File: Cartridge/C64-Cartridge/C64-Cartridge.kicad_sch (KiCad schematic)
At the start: 22 parts, among them J1 C64_Expansion_port, J2 GND, SW1 SW_DIP_x08, SW2 RESET, SW3 RESET, U1 SST39SF040

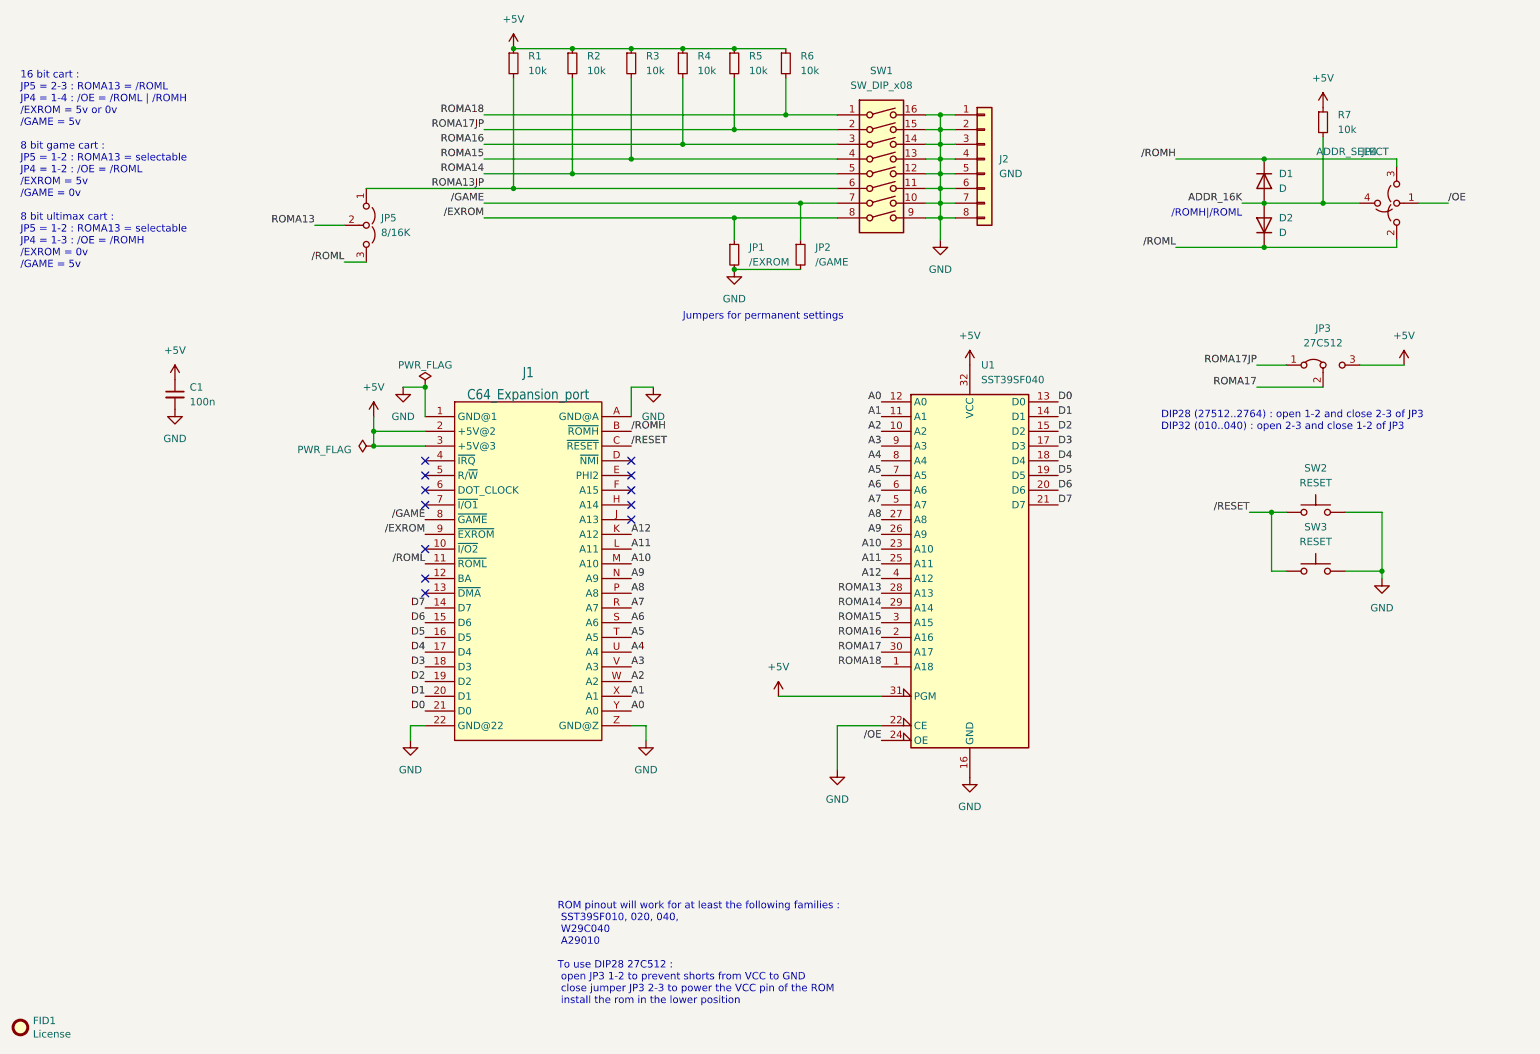
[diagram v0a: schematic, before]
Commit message: C64-Cartridge : addition of EpyxFastload daughter board ; some silkscreen changes. C64-KungFuFlash, C64-Pi1541 : small updates before production. New C64-efuse board that fit inside the DIN plug.
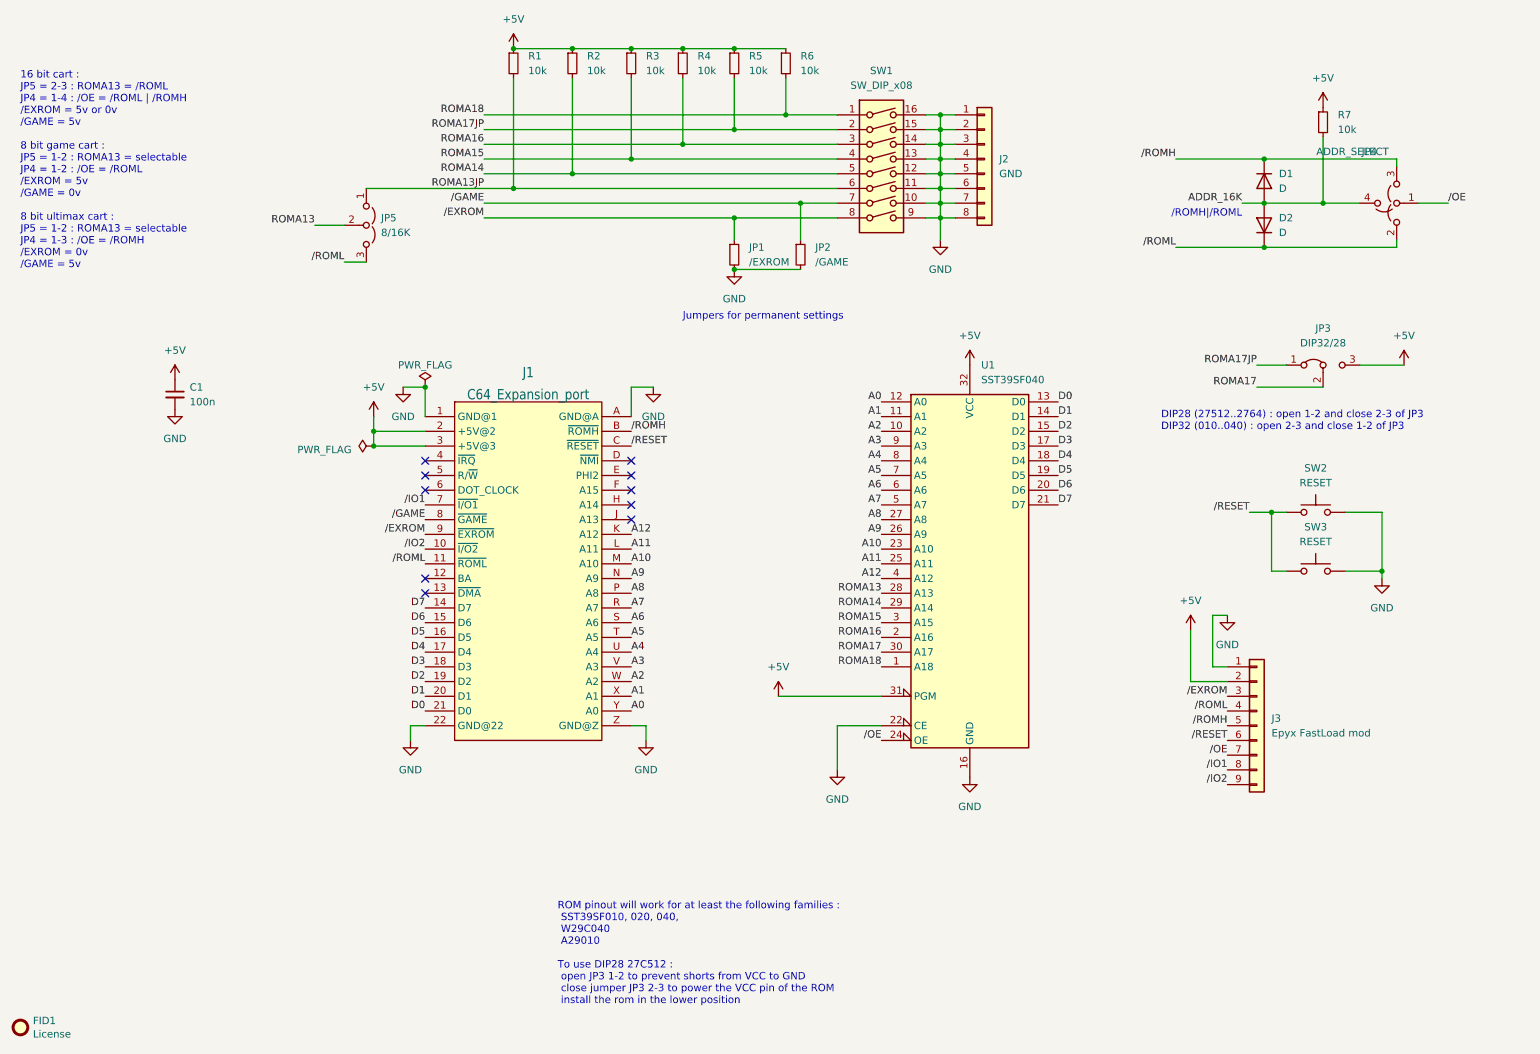
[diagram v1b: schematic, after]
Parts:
- added J3: Epyx FastLoad mod, Connector_PinHeader_1.27mm:PinHeader_1x09_P1.27mm_Vertical, symbol Connector_Generic:Conn_01x09
- JP3: value 27C512 -> DIP32/28; footprint Jumper:SolderJumper-3_P1.3mm_Bridged12_RoundedPad1.0x1.5mm -> Jumper:SolderJumper-3_P1.3mm_Open_RoundedPad1.0x1.5mm
- R1, R2, R3: footprint Sassa:C_0805_2012Metric_shortable -> Resistor_SMD:R_0805_2012Metric
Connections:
- net +5V: now also J3.2 (Pin_2)
- net GND: now also J3.1 (Pin_1)
- net /EXROM: now also J3.3 (Pin_3)
- net /OE: now also J3.7 (Pin_7)
- net /RESET: now also J3.6 (Pin_6)
- net /ROMH: now also J3.5 (Pin_5)
- net /ROML: now also J3.4 (Pin_4)
- net /IO2: now reaches J1.10 (~{I/O2})
- net /IO2: now also J3.9 (Pin_9)
- net /IO1: now reaches J1.7 (~{I/O1})
- net /IO1: now also J3.8 (Pin_8)
- no-connect marks 12 -> 10
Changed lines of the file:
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@@
   (junction (at 124.46 41.91) (diameter 0) (color 0 0 0 0)
   )
-  (no_connect (at 88.9 101.6))
   (no_connect (at 88.9 99.06))
   (no_connect (at 124.46 96.52))
-  (no_connect (at 88.9 109.22))
   (no_connect (at 88.9 93.98))
   (no_connect (at 88.9 116.84))
@@
     (stroke (width 0) (type default))
   )
+  (wire (pts (xy 227.33 129.54) (xy 224.79 129.54))
+    (stroke (width 0) (type default))
+  )
   (wire (pts (xy 177.8 44.45) (xy 180.34 44.45))
     (stroke (width 0) (type default))
@@
     (stroke (width 0) (type default))
   )
+  (wire (pts (xy 224.79 120.65) (xy 227.33 120.65))
+    (stroke (width 0) (type default))
+  )
   (wire (pts (xy 160.02 139.7) (xy 160.02 147.32))
     (stroke (width 0) (type default))
@@
     (stroke (width 0) (type default))
   )
+  (wire (pts (xy 224.79 129.54) (xy 224.79 120.65))
+    (stroke (width 0) (type default))
+  )
   (wire (pts (xy 260.35 49.53) (xy 265.43 49.53))
     (stroke (width 0) (type default))
@@
     (stroke (width 0) (type default))
   )
+  (wire (pts (xy 220.98 132.08) (xy 220.98 123.19))
+    (stroke (width 0) (type default))
+  )
   (wire (pts (xy 247.65 113.03) (xy 254 113.03))
     (stroke (width 0) (type default))
@@
   )
   (wire (pts (xy 124.46 41.91) (xy 160.02 41.91))
+    (stroke (width 0) (type default))
+  )
+  (wire (pts (xy 227.33 132.08) (xy 220.98 132.08))
     (stroke (width 0) (type default))
   )
@@
     (effects (font (size 1.27 1.27)) (justify right bottom))
   )
+  (label "{slash}IO1" (at 227.33 147.32 180) (fields_autoplaced)
+    (effects (font (size 1.27 1.27)) (justify right bottom))
+  )
   (label "A7" (at 167.64 101.6 180) (fields_autoplaced)
     (effects (font (size 1.27 1.27)) (justify right bottom))
@@
     (effects (font (size 1.27 1.27)) (justify right bottom))
   )
+  (label "{slash}ROML" (at 227.33 137.16 180) (fields_autoplaced)
+    (effects (font (size 1.27 1.27)) (justify right bottom))
+  )
+  (label "{slash}IO2" (at 227.33 149.86 180) (fields_autoplaced)
+    (effects (font (size 1.27 1.27)) (justify right bottom))
+  )
   (label "A12" (at 167.64 114.3 180) (fields_autoplaced)
     (effects (font (size 1.27 1.27)) (justify right bottom))
   )
+  (label "{slash}OE" (at 227.33 144.78 180) (fields_autoplaced)
+    (effects (font (size 1.27 1.27)) (justify right bottom))
+  )
+  (label "{slash}IO1" (at 88.9 101.6 180) (fields_autoplaced)
+    (effects (font (size 1.27 1.27)) (justify right bottom))
+  )
   (label "D7" (at 198.12 101.6 0) (fields_autoplaced)
     (effects (font (size 1.27 1.27)) (justify left bottom))
@@
     (effects (font (size 1.27 1.27)) (justify left bottom))
   )
+  (label "{slash}RESET" (at 227.33 142.24 180) (fields_autoplaced)
+    (effects (font (size 1.27 1.27)) (justify right bottom))
+  )
   (label "{slash}EXROM" (at 88.9 106.68 180) (fields_autoplaced)
     (effects (font (size 1.27 1.27)) (justify right bottom))
@@
     (effects (font (size 1.27 1.27)) (justify right bottom))
   )
+  (label "{slash}ROMH" (at 227.33 139.7 180) (fields_autoplaced)
+    (effects (font (size 1.27 1.27)) (justify right bottom))
+  )
   (label "ROMA17JP" (at 232.41 77.47 180) (fields_autoplaced)
     (effects (font (size 1.27 1.27)) (justify right bottom))
   )
+  (label "{slash}IO2" (at 88.9 109.22 180) (fields_autoplaced)
+    (effects (font (size 1.27 1.27)) (justify right bottom))
+  )
   (label "D6" (at 198.12 99.06 0) (fields_autoplaced)
     (effects (font (size 1.27 1.27)) (justify left bottom))
@@
     (effects (font (size 1.27 1.27)) (justify left bottom))
   )
+  (label "{slash}EXROM" (at 227.33 134.62 180) (fields_autoplaced)
+    (effects (font (size 1.27 1.27)) (justify right bottom))
+  )
   (label "ROMA13" (at 167.64 116.84 180) (fields_autoplaced)
     (effects (font (size 1.27 1.27)) (justify right bottom))
@@
   (label "A2" (at 167.64 88.9 180) (fields_autoplaced)
     (effects (font (size 1.27 1.27)) (justify right bottom))
+  )
+  (symbol (lib_id "power:GND") (at 227.33 120.65 0) (unit 1)
+    (in_bom yes) (on_board yes) (dnp no) (fields_autoplaced)
+    (property "Reference" "#PWR018" (at 227.33 127 0)
+      (effects (font (size 1.27 1.27)) hide)
+    )
+    (property "Value" "GND" (at 227.33 125.73 0)
+      (effects (font (size 1.27 1.27)))
+    )
+    (property "Footprint" "" (at 227.33 120.65 0)
+      (effects (font (size 1.27 1.27)) hide)
+    )
+    (property "Datasheet" "" (at 227.33 120.65 0)
+      (effects (font (size 1.27 1.27)) hide)
+    )
+    (pin "1")
+    (instances
+      (project "C64-Cartridge"
+        (path "/66dece7b-bdc9-4b2c-8738-7ab5a5409aa2"
+          (reference "#PWR018") (unit 1)
+        )
+      )
+    )
   )
   (symbol (lib_id "power:GND") (at 182.88 148.59 0) (unit 1)
@@
       (effects (font (size 1.27 1.27)) (justify left))
     )
-    (property "Footprint" "Sassa:C_0805_2012Metric_shortable" (at 124.46 25.4 0)
+    (property "Footprint" "Resistor_SMD:R_0805_2012Metric" (at 124.46 25.4 0)
       (effects (font (size 1.27 1.27)) hide)
     )
@@
         (path "/66dece7b-bdc9-4b2c-8738-7ab5a5409aa2"
           (reference "R3") (unit 1)
+        )
+      )
+    )
+  )
+  (symbol (lib_id "power:+5V") (at 220.98 123.19 0) (unit 1)
+    (in_bom yes) (on_board yes) (dnp no) (fields_autoplaced)
+    (property "Reference" "#PWR019" (at 220.98 127 0)
+      (effects (font (size 1.27 1.27)) hide)
+    )
+    (property "Value" "+5V" (at 220.98 118.11 0)
+      (effects (font (size 1.27 1.27)))
+    )
+    (property "Footprint" "" (at 220.98 123.19 0)
+      (effects (font (size 1.27 1.27)) hide)
+    )
+    (property "Datasheet" "" (at 220.98 123.19 0)
+      (effects (font (size 1.27 1.27)) hide)
+    )
+    (pin "1")
+    (instances
+      (project "C64-Cartridge"
+        (path "/66dece7b-bdc9-4b2c-8738-7ab5a5409aa2"
+          (reference "#PWR019") (unit 1)
         )
       )
@@
       (effects (font (size 1.27 1.27)))
     )
-    (property "Value" "27C512" (at 243.84 73.66 0)
-      (effects (font (size 1.27 1.27)))
-    )
-    (property "Footprint" "Jumper:SolderJumper-3_P1.3mm_Bridged12_RoundedPad1.0x1.5mm" (at 243.84 77.47 0)
+    (property "Value" "DIP32/28" (at 243.84 73.66 0)
+      (effects (font (size 1.27 1.27)))
+    )
+    (property "Footprint" "Jumper:SolderJumper-3_P1.3mm_Open_RoundedPad1.0x1.5mm" (at 243.84 77.47 0)
       (effects (font (size 1.27 1.27)) hide)
     )
@@
         (path "/66dece7b-bdc9-4b2c-8738-7ab5a5409aa2"
           (reference "#PWR03") (unit 1)
+        )
+      )
+    )
+  )
+  (symbol (lib_id "Connector_Generic:Conn_01x09") (at 232.41 139.7 0) (unit 1)
+    (in_bom yes) (on_board yes) (dnp no) (fields_autoplaced)
+    (property "Reference" "J3" (at 234.95 138.43 0)
+      (effects (font (size 1.27 1.27)) (justify left))
+    )
+    (property "Value" "Epyx FastLoad mod" (at 234.95 140.97 0)
+      (effects (font (size 1.27 1.27)) (justify left))
+    )
+    (property "Footprint" "Connector_PinHeader_1.27mm:PinHeader_1x09_P1.27mm_Vertical" (at 232.41 139.7 0)
+      (effects (font (size 1.27 1.27)) hide)
+    )
+    (property "Datasheet" "~" (at 232.41 139.7 0)
+      (effects (font (size 1.27 1.27)) hide)
+    )
+    (pin "1")
+    (pin "2")
+    (pin "3")
+    (pin "4")
+    (pin "5")
+    (pin "6")
+    (pin "7")
+    (pin "8")
+    (pin "9")
+    (instances
+      (project "C64-Cartridge"
+        (path "/66dece7b-bdc9-4b2c-8738-7ab5a5409aa2"
+          (reference "J3") (unit 1)
         )
       )
@@
       (effects (font (size 1.27 1.27)) (justify left))
     )
-    (property "Footprint" "Sassa:C_0805_2012Metric_shortable" (at 114.3 25.4 0)
+    (property "Footprint" "Resistor_SMD:R_0805_2012Metric" (at 114.3 25.4 0)
       (effects (font (size 1.27 1.27)) hide)
     )
@@
       (effects (font (size 1.27 1.27)) (justify left))
     )
-    (property "Footprint" "Sassa:C_0805_2012Metric_shortable" (at 104.14 25.4 0)
-      (effects (font (size 1.27 1.27)) hide)
-    )
+    (property "Footprint" "Resistor_SMD:R_0805_2012Metric" (at 104.14 25.4 0)
+      (effects (font (size 1.27 1.27)) hide)
+    )
